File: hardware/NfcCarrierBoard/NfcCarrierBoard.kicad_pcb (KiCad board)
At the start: 2 copper layers, 60 x 80 mm, 3 parts

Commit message: Begin work on PCB layout
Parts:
- removed A3: ~, FootprintLibrary:WIZnet Ethernet HAT
- added A4: 5V 3A Buck Reg, FootprintLibrary:SparkFun BabyBuck Regulator 5V, F.Cu at (169.3, 74.5)
- added BZ1: Buzzer, FootprintLibrary:Buzzer_PUIaudio_AT-1224-TWT_D12_H9_6.5mm, F.Cu at (39.2, 129.0)
- added C1: 10µF, FootprintLibrary:SMD_HANDSOLDER_UNIVERSAL_0603_0805_1206, F.Cu at (39.0, 140.0)
- added C10: 0.1µF, FootprintLibrary:SMD_HANDSOLDER_UNIVERSAL_0603_0805_1206, F.Cu at (159.9, 83.0)
- added C2: 0.1µF, FootprintLibrary:SMD_HANDSOLDER_UNIVERSAL_0603_0805_1206, F.Cu at (86.5, 175.9)
- added C3: 0.1µF, FootprintLibrary:SMD_HANDSOLDER_UNIVERSAL_0603_0805_1206, F.Cu at (119.3, 54.5)
- added C4: 0.1µF, FootprintLibrary:SMD_HANDSOLDER_UNIVERSAL_0603_0805_1206, F.Cu at (39.0, 149.0)
- added C5: 0.1µF, FootprintLibrary:SMD_HANDSOLDER_UNIVERSAL_0603_0805_1206, F.Cu at (323.3, 84.5)
- added C6: 0.1µF, FootprintLibrary:SMD_HANDSOLDER_UNIVERSAL_0603_0805_1206, F.Cu at (19.6, 188.7)
- added C7: 0.1µF, FootprintLibrary:SMD_HANDSOLDER_UNIVERSAL_0603_0805_1206, F.Cu at (131.1, 58.7)
- added C8: 0.1µF, FootprintLibrary:SMD_HANDSOLDER_UNIVERSAL_0603_0805_1206, F.Cu at (118.3, 98.2)
- added C9: 0.1µF, FootprintLibrary:SMD_HANDSOLDER_UNIVERSAL_0603_0805_1206, F.Cu at (150.0, 68.1)
- added D1: SL54A, FootprintLibrary:SMD_HANDSOLDER_UNIVERSAL_0603_0805_1206, F.Cu at (168.6, 67.5)
- added D2: SL54A, FootprintLibrary:SMD_HANDSOLDER_UNIVERSAL_0603_0805_1206, F.Cu at (30.8, 150.2)
- added D3: WS2812B, LED_SMD:LED_WS2812B_PLCC4_5.0x5.0mm_P3.2mm, F.Cu at (86.7, 181.5)
- added H1: MountingHole, MountingHole:MountingHole_3.2mm_M3, F.Cu at (105.0, 55.0)
- added H2: MountingHole, MountingHole:MountingHole_3.2mm_M3, F.Cu at (175.0, 55.0)
- added H3: MountingHole, MountingHole:MountingHole_3.2mm_M3, F.Cu at (105.0, 145.0)
- added H4: MountingHole, MountingHole:MountingHole_3.2mm_M3, F.Cu at (175.0, 145.0)
- added J1: Barrel_Jack, Connector_BarrelJack:BarrelJack_Horizontal, F.Cu at (166.1, 61.5)
- added J2: Conn_01x03, Connector_PinHeader_2.54mm:PinHeader_1x03_P2.54mm_Vertical, F.Cu at (96.0, 173.7)
- added J3: JST SH 4, FootprintLibrary:JST-SH-4-top, F.Cu at (308.1, 80.2)
- added J4: Grove, Connector:NS-Tech_Grove_1x04_P2mm_Vertical, F.Cu at (317.0, 77.0)
- added J5: Conn_01x03, Connector_PinHeader_2.54mm:PinHeader_1x03_P2.54mm_Vertical, F.Cu at (26.0, 184.5)
- added J6: UART, Connector_PinHeader_2.54mm:PinHeader_1x04_P2.54mm_Vertical, F.Cu at (318.0, 111.2)
- added J7: Grove UART, Connector:NS-Tech_Grove_1x04_P2mm_Vertical, F.Cu at (311.0, 111.4)
- added JP1: SolderJumper_2_Bridged, Jumper:SolderJumper-2_P1.3mm_Bridged_RoundedPad1.0x1.5mm, F.Cu at (325.4, 202.9)
- added JP2: SolderJumper_2_Bridged, Jumper:SolderJumper-2_P1.3mm_Bridged_RoundedPad1.0x1.5mm, F.Cu at (325.4, 206.5)
- added JP3: SolderJumper_3_Bridged12, Jumper:SolderJumper-3_P1.3mm_Bridged12_RoundedPad1.0x1.5mm, F.Cu at (50.3, 138.3)
- added JP4: SolderJumper_2_Open, Jumper:SolderJumper-2_P1.3mm_Open_RoundedPad1.0x1.5mm, F.Cu at (49.6, 127.0)
- added Q1: NMOS, Package_TO_SOT_SMD:SOT-323_SC-70_Handsoldering, F.Cu at (50.4, 130.8)
- added Q2: NMOS, Package_TO_SOT_SMD:SOT-323_SC-70_Handsoldering, F.Cu at (91.8, 173.4)
- added R1: ~10kΩ, FootprintLibrary:SMD_HANDSOLDER_UNIVERSAL_0603_0805_1206, F.Cu at (23.3, 135.0)
- added R2: 330Ω, FootprintLibrary:SMD_HANDSOLDER_UNIVERSAL_0603_0805_1206, F.Cu at (30.0, 139.1)
- added R3: ~10Ω, FootprintLibrary:SMD_HANDSOLDER_UNIVERSAL_0603_0805_1206, F.Cu at (30.0, 142.0)
- added R4: 10kΩ, FootprintLibrary:SMD_HANDSOLDER_UNIVERSAL_0603_0805_1206, F.Cu at (323.8, 77.7)
- added R5: 10kΩ, FootprintLibrary:SMD_HANDSOLDER_UNIVERSAL_0603_0805_1206, F.Cu at (323.8, 80.6)
- added R6: 10kΩ, FootprintLibrary:SMD_HANDSOLDER_UNIVERSAL_0603_0805_1206, F.Cu at (78.4, 173.1)
- added R7: 10kΩ, FootprintLibrary:SMD_HANDSOLDER_UNIVERSAL_0603_0805_1206, F.Cu at (78.4, 176.0)
- added R8: 4.7kΩ, FootprintLibrary:SMD_HANDSOLDER_UNIVERSAL_0603_0805_1206, F.Cu at (20.0, 183.6)
- added RV1: R_Potentiometer_Trim, Potentiometer_THT:Potentiometer_Runtron_RM-065_Vertical, F.Cu at (46.0, 146.0)
- added SW1: RESET, FootprintLibrary:SW_TS11-674-105-BK-260-RA-D, F.Cu at (153.4, 56.7)
- added TP1: TestPoint, TestPoint:TestPoint_Pad_D2.0mm, F.Cu at (108.7, 110.8)
- added TP10: TestPoint, TestPoint:TestPoint_Pad_D2.0mm, F.Cu at (139.5, -3.60)
- added TP2: TestPoint, TestPoint:TestPoint_Pad_D2.0mm, F.Cu at (112.1, 110.9)
- added TP3: TestPoint, TestPoint:TestPoint_Pad_D2.0mm, F.Cu at (135.5, -11.7)
- added TP4: TestPoint, TestPoint:TestPoint_Pad_D2.0mm, F.Cu at (135.5, -7.65)
- added TP5: TestPoint, TestPoint:TestPoint_Pad_D2.0mm, F.Cu at (135.5, -3.60)
- added TP6: TestPoint, TestPoint:TestPoint_Pad_D2.0mm, F.Cu at (139.5, -19.8)
- added TP7: TestPoint, TestPoint:TestPoint_Pad_D2.0mm, F.Cu at (139.5, -15.8)
- added TP8: TestPoint, TestPoint:TestPoint_Pad_D2.0mm, F.Cu at (139.5, -11.7)
- added TP9: TestPoint, TestPoint:TestPoint_Pad_D2.0mm, F.Cu at (139.5, -7.65)
- added U1: 24AA02E-OT, Package_TO_SOT_SMD:SOT-23-5, F.Cu at (330.6, 205.4)
- A2: value ~ -> Ethernet FeatherWing; footprint Module:Adafruit_Feather -> FootprintLibrary:Adafruit_Ethernet_FeatherWing
- moved A1 9.29 mm to (126.6, 54.5)
- moved A2 1.36 mm to (123.1, 100.8)
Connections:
- A1 pad 10: unconnected-(A1-A5*-Pad10) -> Net-(A1-A5*)
- A1 pad 14: unconnected-(A1-RX-Pad14) -> RX
- A1 pad 15: unconnected-(A1-TX-Pad15) -> TX
- A1 pad 17: unconnected-(A1-SDA-Pad17) -> SDA
- A1 pad 18: unconnected-(A1-SCL-Pad18) -> SCL
- A1 pad 19: unconnected-(A1-D5-Pad19) -> BUZZER
- A1 pad 20: unconnected-(A1-D6-Pad20) -> Net-(A1-D6)
- A1 pad 21: unconnected-(A1-D9-Pad21) -> 1-Wire DQ
- A1 pad 23: unconnected-(A1-D11-Pad23) -> Ethernet ~{RST}
- A1 pad 24: unconnected-(A1-D12-Pad24) -> Ethernet ~{IRQ}
- A1 pad 25: unconnected-(A1-D13-Pad25) -> NEO_DI_LV
- A1 pad 26: VBUS -> +5V
- A1 pad 3: unconnected-(A1-AREF-Pad3) -> Net-(A1-AREF)
- A1 pad 5: unconnected-(A1-A0-Pad5) -> Net-(A1-A0)
- A1 pad 6: unconnected-(A1-A1-Pad6) -> Net-(A1-A1)
- A1 pad 7: unconnected-(A1-A2-Pad7) -> Net-(A1-A2)
- A1 pad 8: unconnected-(A1-A3-Pad8) -> Net-(A1-A3)
- A1 pad 9: unconnected-(A1-A4*-Pad9) -> Net-(A1-A4*)
- A2 pad 17: unconnected-(A2-Pad17) -> SDA
- A2 pad 18: unconnected-(A2-Pad18) -> SCL
- A2 pad 21: SDI -> unconnected-(A2-Pad21)
- A2 pad 24: unconnected-(A2-Pad24) -> Ethernet ~{IRQ}
- A2 pad 26: unconnected-(A2-Pad26) -> +5V
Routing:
- net +5V: track 0.00 -> 96.5 mm
- net VBUS: track 91.0 -> 0.00 mm
- net Ethernet ~{IRQ}: track 0.00 -> 56.7 mm
- net Ethernet ~{CS}: track 82.9 -> 47.6 mm
- net ~{RESET}: track 66.0 -> 31.1 mm
- net SDO: track 36.4 -> 8.51 mm
- net +3.3V: track 80.7 -> 54.6 mm
- net SCK: track 38.5 -> 15.6 mm
- net +12V: track 0.00 -> 22.2 mm
- net SDI: track 37.7 -> 18.6 mm
- net +12V Input: track 0.00 -> 5.34 mm
- net GND: track 1.27 -> 0.00 mm
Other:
- board size 60 x 80 mm -> 80 x 100 mm
- board text added: "I^{2}C"
- board text added: "UART"

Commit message: Populate more of the PCB Some DRC fixes
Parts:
- moved R8 214.1 mm to (229.2, 138.2), turned to 90 degrees
- moved C6 212.0 mm to (226.2, 141.2), turned to -90 degrees
- moved J5 203.1 mm to (222.9, 135.0)
- moved U1 183.0 mm to (174.0, 110.7), turned to -90 degrees
- moved JP1 180.4 mm to (172.8, 106.7), turned to 90 degrees
- moved JP2 180.3 mm to (175.3, 106.7), turned to 90 degrees
- moved C5 153.3 mm to (170.8, 99.5), turned to -90 degrees
- moved R4 152.0 mm to (172.6, 92.5), turned to 180 degrees
- moved R5 152.0 mm to (172.6, 95.2), turned to 180 degrees
- moved J4 151.7 mm to (166.2, 94.2)
- moved J3 150.8 mm to (158.2, 97.0)
- moved R1 95.9 mm to (118.1, 120.4), turned to -90 degrees
- moved R2 93.6 mm to (121.0, 117.1), turned to -90 degrees
- moved D2 89.2 mm to (114.9, 120.4), turned to 90 degrees
- moved R3 83.0 mm to (112.2, 130.2)
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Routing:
- net +5V: track 96.5 -> 218.7 mm, vias 0 -> 7
- net +3.3V: track 54.6 -> 166.2 mm
- net NEO_DI_LV: track 0.00 -> 78.1 mm
- net SCL: track 0.00 -> 54.3 mm
- net BUZZER: track 0.00 -> 52.0 mm, vias 0 -> 2
- net SDA: track 0.00 -> 48.9 mm, vias 0 -> 1
- net Net-(BZ1-+): track 0.00 -> 19.2 mm
- net NEO_DI: track 0.00 -> 19.1 mm
- net Net-(BZ1--): track 0.00 -> 11.4 mm
- net NEO_DO: track 0.00 -> 9.66 mm
- net Net-(JP4-B): track 0.00 -> 7.99 mm
- net 1-Wire DQ: track 0.00 -> 6.70 mm
- net Net-(Q1-G): track 0.00 -> 5.14 mm
- net Net-(JP3-C): track 0.00 -> 5.07 mm
- net SCK: track 15.6 -> 18.5 mm
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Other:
- outline, holes or cut-outs redrawn
- board text added: "1-Wire"
- board text added: "Challenger RP2040 NFC"
- board text added: "Ethernet FeatherWing"
- board text added: "MAC Address (EEPROM)"
- board text added: "NeoPixel"
- board text added: "PC Speaker"
- board text added: "Unused pins"
- board text added: "Volume"

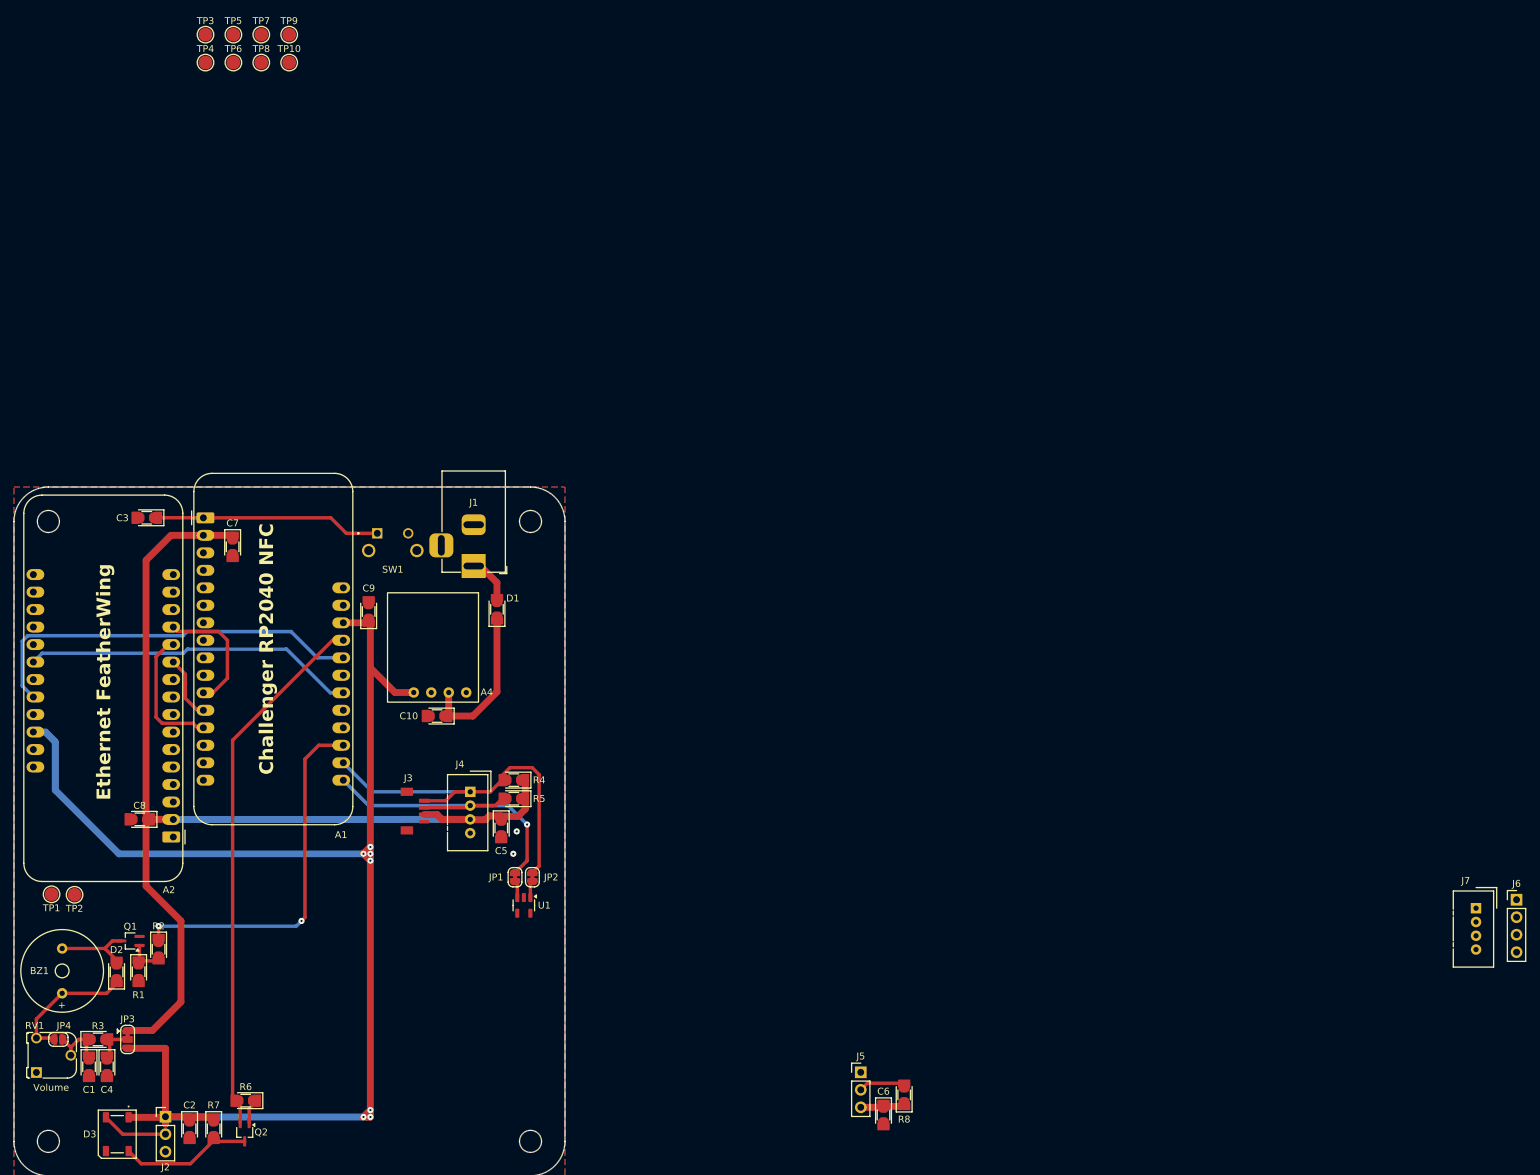
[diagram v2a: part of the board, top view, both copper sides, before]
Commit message: Place last components
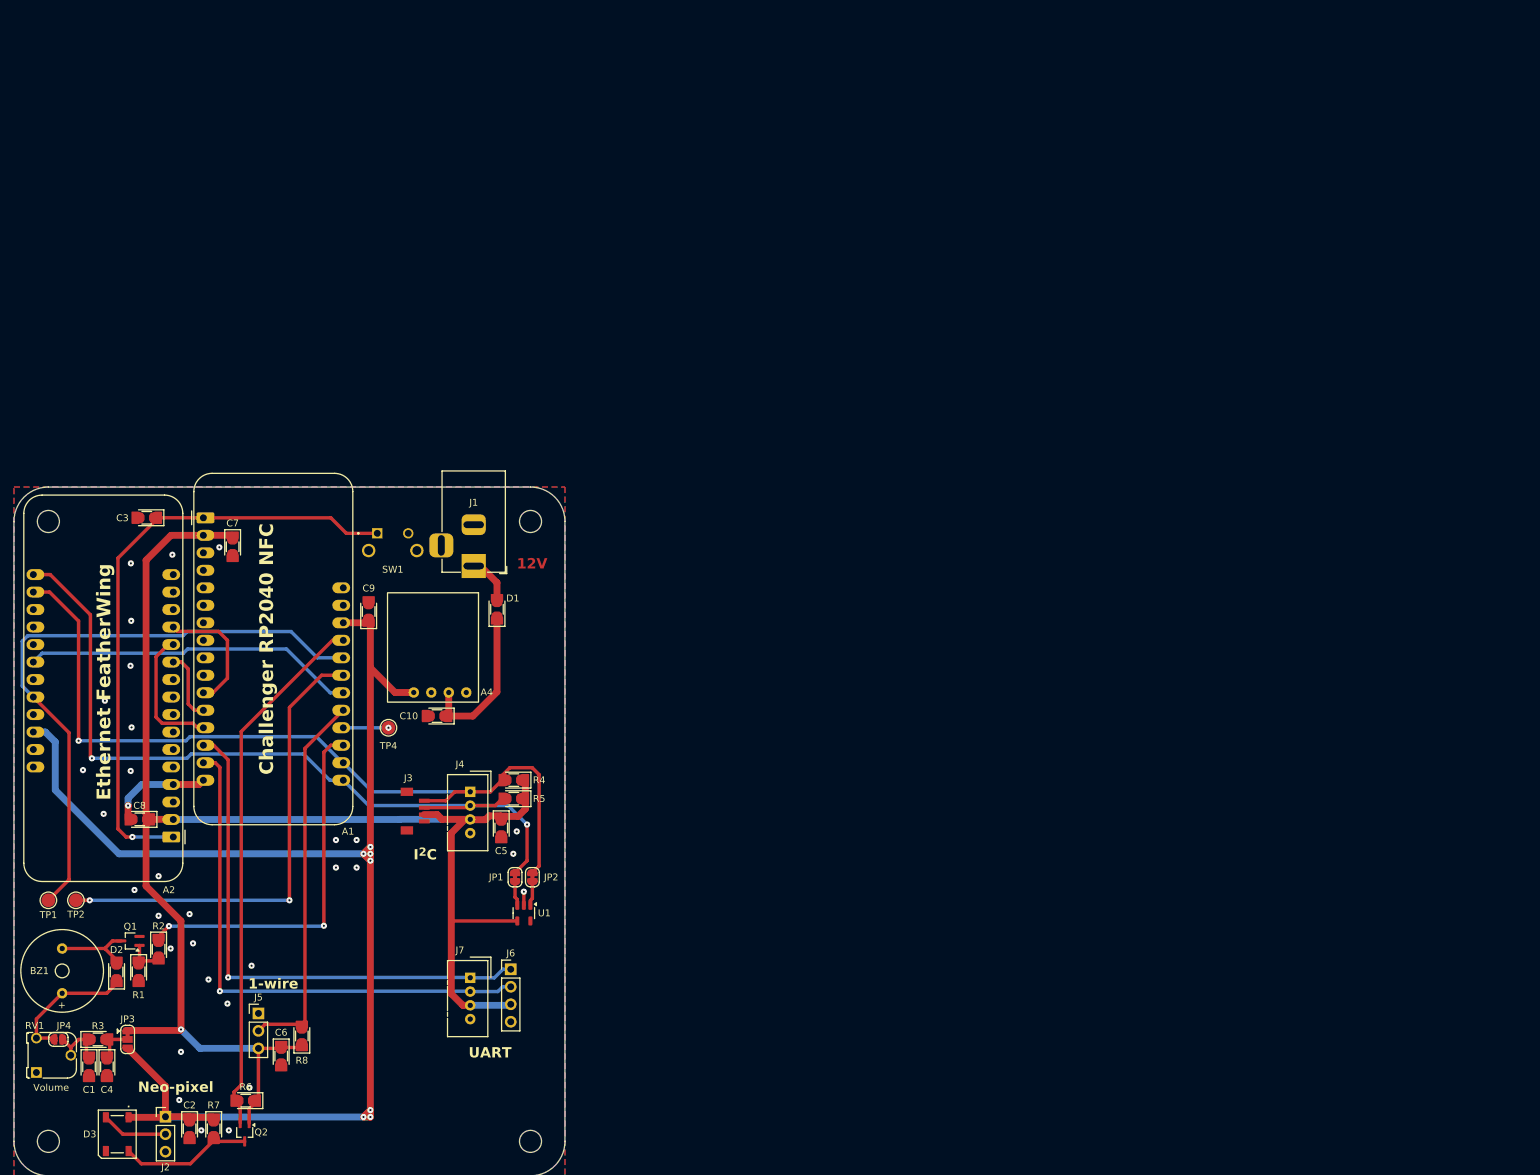
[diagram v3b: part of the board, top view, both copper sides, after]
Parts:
- removed TP10, TP3, TP5, TP6, TP7, TP8, TP9: TestPoint, TestPoint:TestPoint_Pad_D2.0mm
- moved J6 146.4 mm to (172.1, 120.0)
- moved J7 146.4 mm to (166.2, 121.2)
- moved TP4 100.2 mm to (154.4, 85.0)
- moved C6 87.9 mm to (138.8, 132.6)
- moved J5 87.9 mm to (135.5, 126.4)
- moved R8 87.9 mm to (141.8, 129.7)
- moved U1 1.12 mm to (174.0, 111.9)
- moved TP1 0.98 mm to (105.0, 110.0)
- moved TP2 0.82 mm to (109.0, 110.0)
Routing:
- net TX: track 0.00 -> 77.7 mm, vias 0 -> 1
- net RX: track 0.00 -> 77.6 mm, vias 0 -> 1
- net SDA: track 48.9 -> 118.9 mm, vias 1 -> 2
- net Ethernet ~{RST}: track 0.00 -> 68.8 mm, vias 0 -> 2
- net +3.3V: track 166.2 -> 234.5 mm, vias 0 -> 1
- net SCL: track 54.3 -> 120.3 mm, vias 0 -> 1
- net ~{RESET}: track 32.7 -> 88.8 mm, vias 0 -> 1
- net 1-Wire DQ: track 6.70 -> 54.8 mm
- net Ethernet ~{IRQ}: track 56.7 -> 89.6 mm
- net GND: track 0.00 -> 17.1 mm, vias 2 -> 32
- net Net-(A1-D6): track 0.00 -> 6.56 mm, vias 0 -> 1
- net +5V: track 218.7 -> 214.4 mm
- net SDO: track 8.51 -> 10.3 mm
- net Net-(JP2-A): track 2.42 -> 3.55 mm
- net Net-(JP1-A): track 2.44 -> 3.56 mm
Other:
- board text added: "1-wire"
- board text added: "12V"
- board text added: "I^{2}C / Quuick / Stemma QT / Grove"
- board text added: "Neo-pixel"
- board text added: "UART / Grove"
- board text removed: "Unused pins"

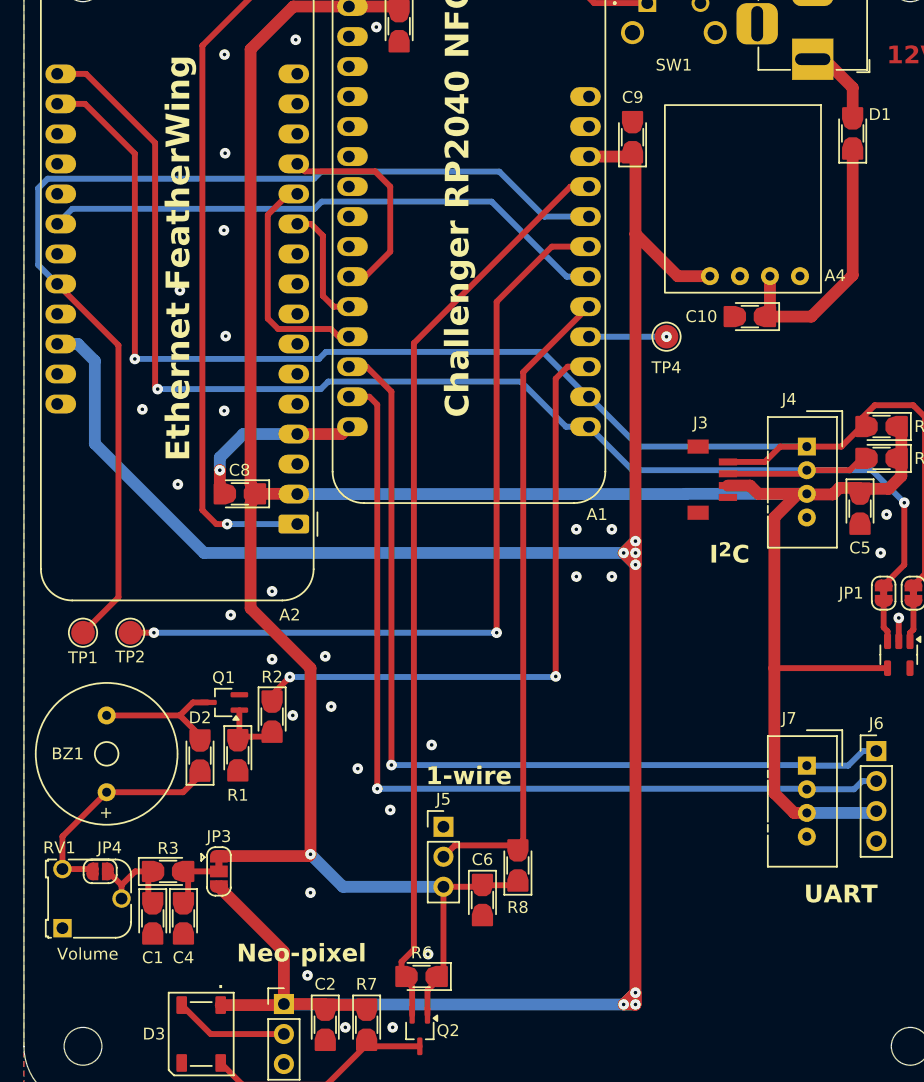
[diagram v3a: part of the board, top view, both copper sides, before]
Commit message: Reduce some sharp angles on signal traces
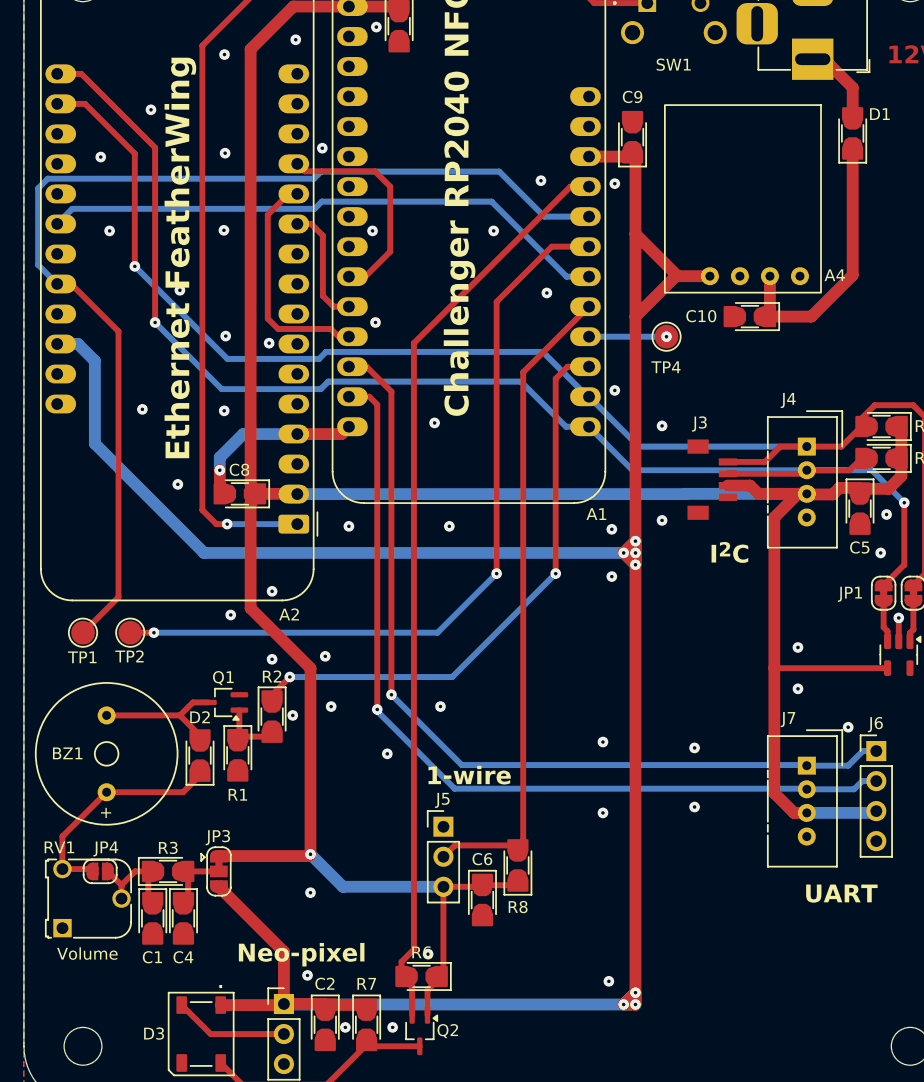
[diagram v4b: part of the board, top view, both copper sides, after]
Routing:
- net BUZZER: track 52.4 -> 47.3 mm
- net +5V: track 214.4 -> 219.4 mm
- net SCL: track 120.3 -> 115.7 mm
- net TX: track 77.7 -> 73.9 mm
- net RX: track 77.6 -> 74.2 mm
- net SDA: track 118.9 -> 115.5 mm
- net Ethernet ~{RST}: track 68.8 -> 65.8 mm
- net Ethernet ~{IRQ}: track 89.6 -> 90.3 mm
- net GND: vias 32 -> 54

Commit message: Add heatsink pad Add silkscreen
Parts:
- added HS1: TestPoint, TestPoint:TestPoint_Pad_D1.0mm, F.Cu at (160.0, 70.0)
- added SYM1: Logo_Open_Hardware_Small, Symbol:OSHW-Logo_19x20mm_SilkScreen, B.Cu at (140.0, 100.0)
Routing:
- net +5V: track 219.4 -> 208.6 mm, vias 7 -> 5
- net +3.3V: track 234.5 -> 233.2 mm
- net Heatsink: vias 0 -> 30
- net GND: vias 54 -> 57
- added copper zone on B.Cu, net Heatsink
- added copper zone on F.Cu, net Heatsink
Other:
- board text added: "${PROJECTNAME} Date: ${ISSUE_DATE} Revision: ${REVISION} ${PROJECT_URL}"
- board text added: "${TITLE}"
